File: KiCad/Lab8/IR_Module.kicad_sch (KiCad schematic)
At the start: 12 parts, among them U1 MCP6294, U2 LM339AN

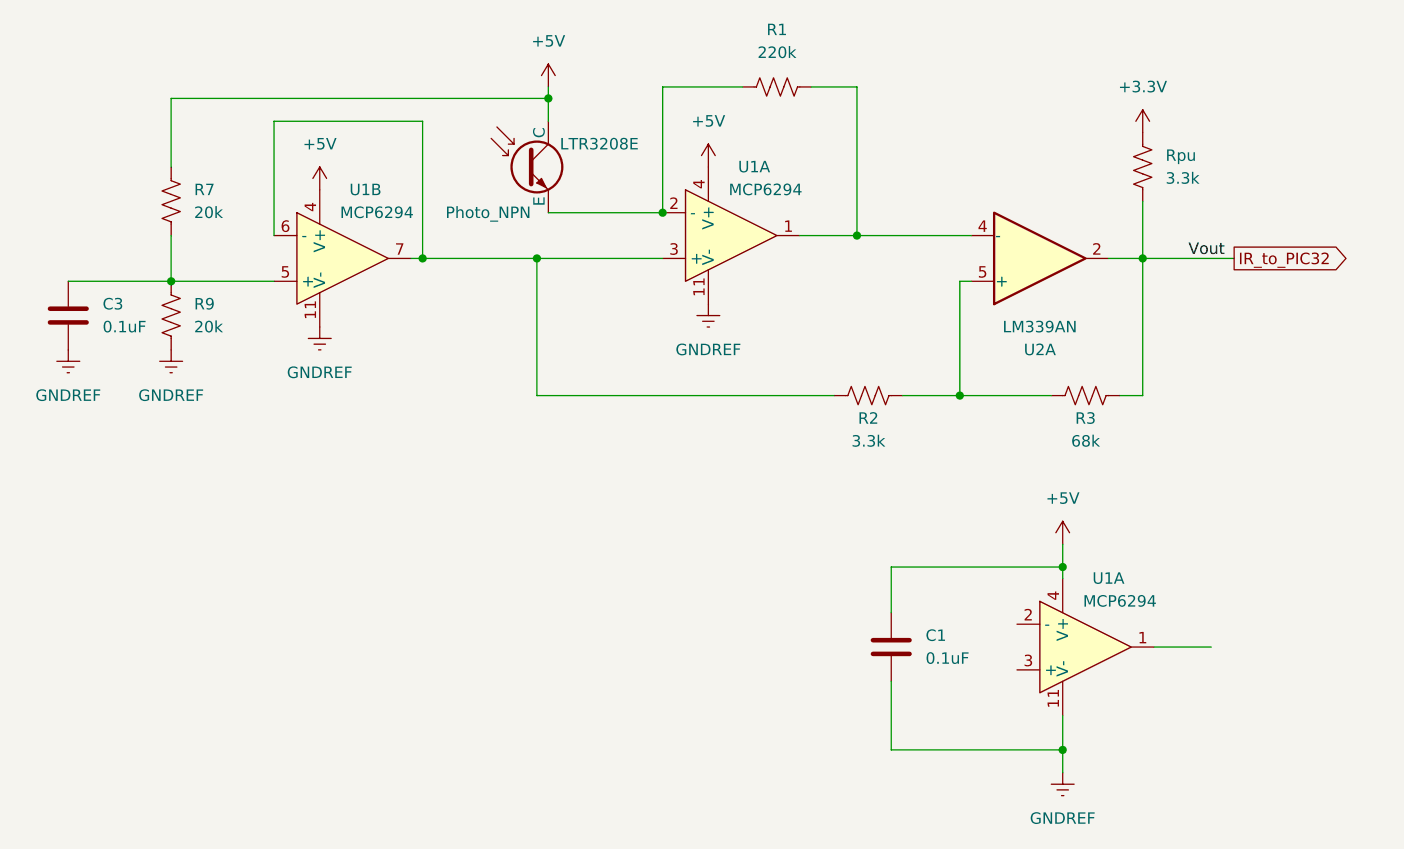
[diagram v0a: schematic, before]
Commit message: Update KiCad, code up beacon detection event checker, disable BeaconDetectService in the project for now
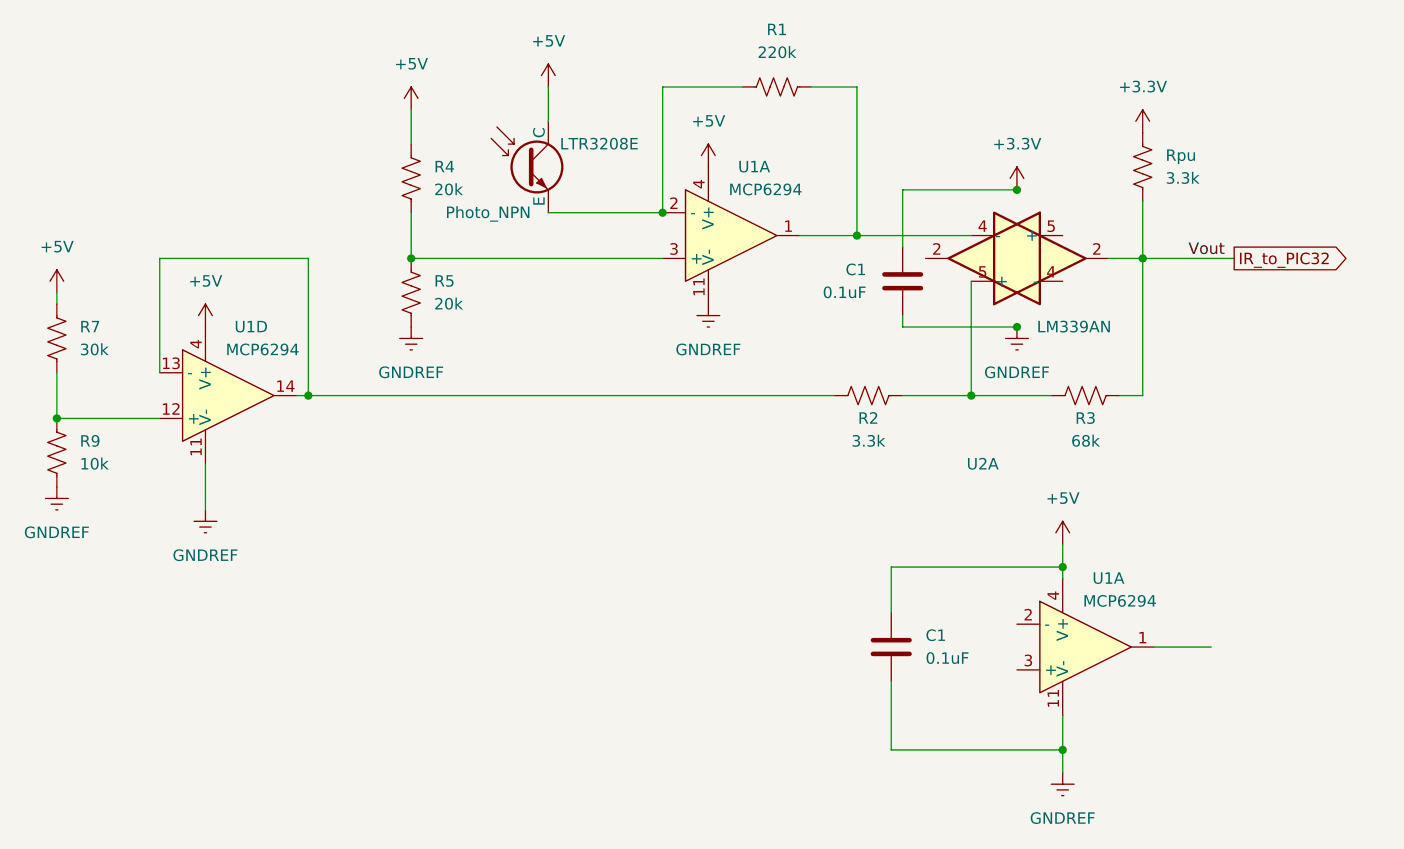
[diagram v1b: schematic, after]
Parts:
- removed C3: 0.1uF, symbol ME218_BaseLib:Cap
- removed unit 2 of U1
- added C1: 0.1uF, symbol ME218_BaseLib:Cap
- added R4, R5: 20k, symbol ME218_BaseLib:Res1
- added unit 4 of U1
- added U2: LM339AN, symbol ME218_BaseLib:LM339AN
- R7: value 20k -> 30k
- R9: value 20k -> 10k
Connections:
- net +3.3V: now also C1.2
- net +5V: now also R4.2, U1.4 (V+)
- net GNDREF: now also C1.1, R5.1, U1.11 (V-)
- net at R2.1: now also U1.13 (-), U1.14; no longer U1.3 (+)
- net at R7.1, R9.2: now also U1.12 (+)
- new net: R4.1, R5.2, U1.3 (+)
